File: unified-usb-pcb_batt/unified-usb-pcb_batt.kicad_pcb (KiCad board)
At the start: 2 copper layers, 30 x 35 mm, 38 parts, among them J1 QI, J2 HRO C-31-M-12, J3 USB_Out, J4 BATT, J5 THERM, SW1 SW_SPDT, U1 SRV05-4, U2 DW01A, U3 TP4056, U4 FS8205

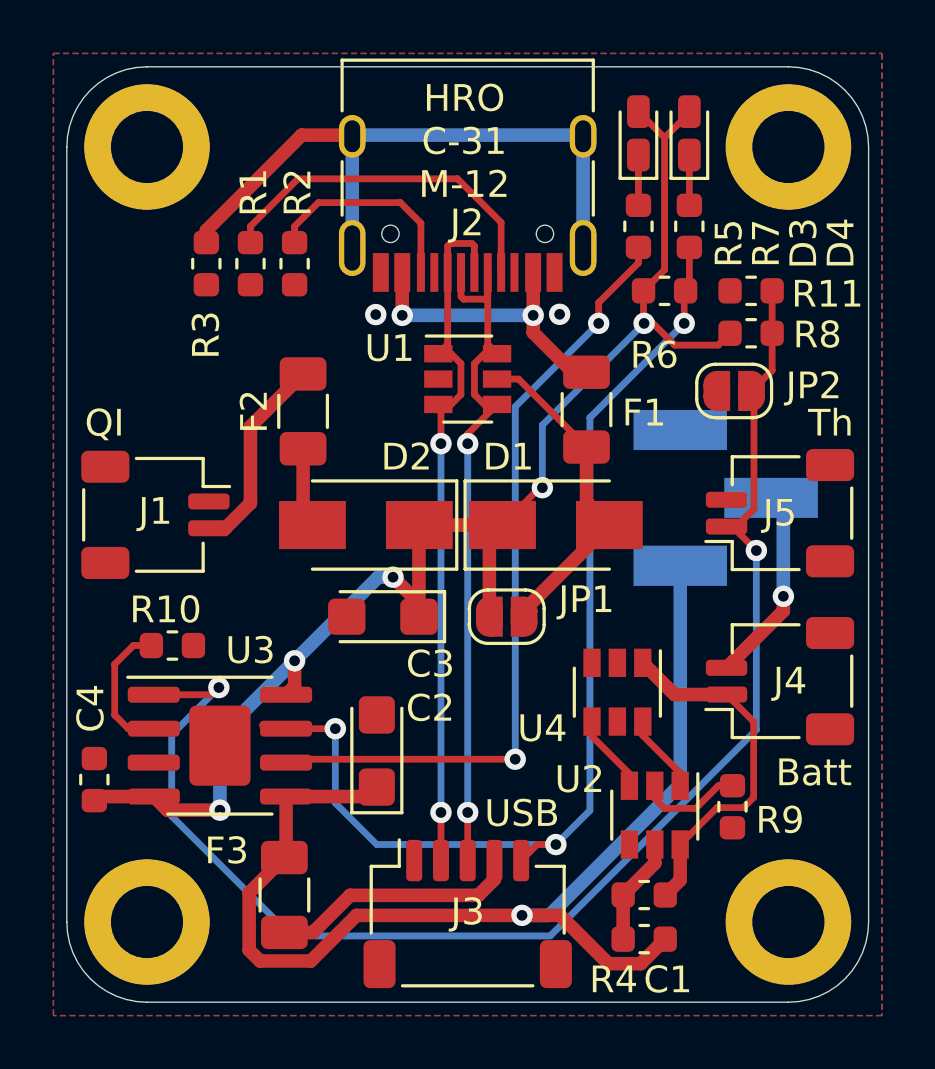
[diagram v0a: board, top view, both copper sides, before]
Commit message: matched usb trace length
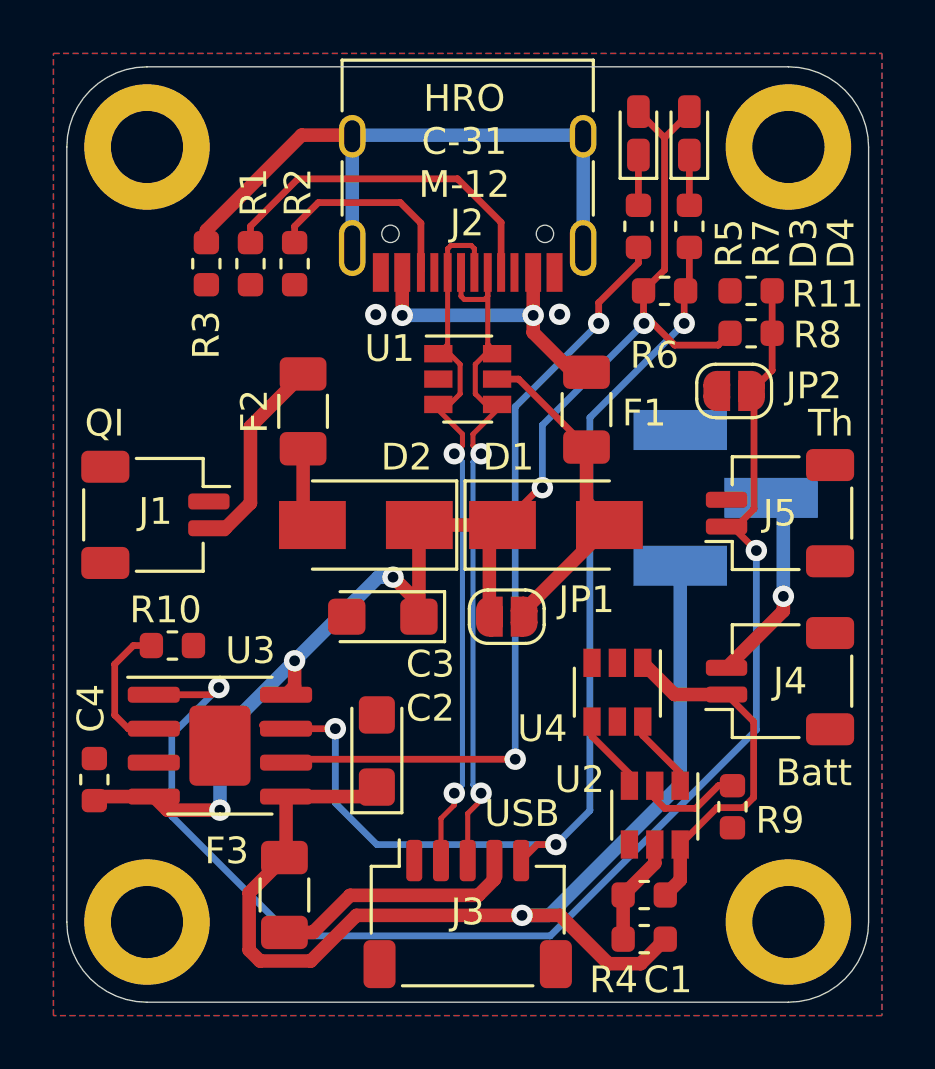
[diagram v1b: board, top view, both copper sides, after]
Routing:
- net USB_D+: track 26.5 -> 27.2 mm
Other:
- net class Default: trace_width 0.254 -> 0.1905
- rule trace_min: 0.2 -> 0.127
- rule via_min_size: 0.4 -> 0.6

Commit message: added ferrite bead
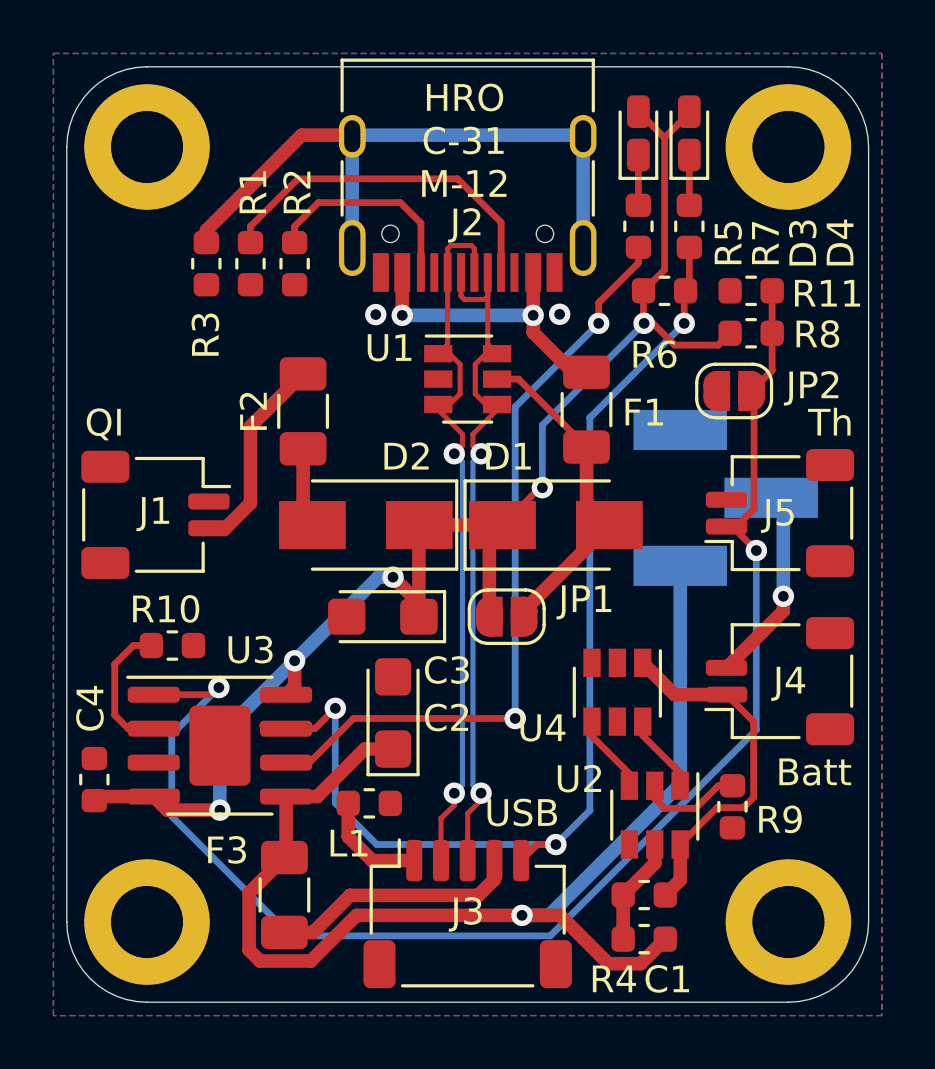
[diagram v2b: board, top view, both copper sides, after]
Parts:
- added L1: BLM18PG121SN1D, Inductor_SMD:L_0603_1608Metric, F.Cu at (27.1, 45.8)
- J2: value HRO C-31-M-12 -> USB_C_Receptacle_USB2.0
- moved C2 1.55 mm to (28.0, 42.5)
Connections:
- J3 pad 1: GNDPWR -> GND
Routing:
- net GND: track 0.00 -> 4.09 mm
- net chgsense: track 39.5 -> 40.6 mm
- net VOUT: track 43.9 -> 44.8 mm
- net Net-(R5-Pad1): track 29.7 -> 29.0 mm
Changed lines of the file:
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@@
     (thickness 1.6)
     (drawings 14)
-    (tracks 229)
+    (tracks 235)
     (zones 0)
-    (modules 38)
-    (nets 32)
+    (modules 39)
+    (nets 33)
   )
   (page A4)
@@
   )
   (setup
-    (last_trace_width 0.1905)
+    (last_trace_width 0.254)
     (user_trace_width 0.254)
     (user_trace_width 0.3048)
@@
   (net 30 "Net-(SW1-Pad1)")
   (net 31 "Net-(J4-Pad2)")
+  (net 32 GND)
   (net_class Default "This is the default net class."
     (clearance 0.1905)
@@
     (diff_pair_width 0.1905)
     (diff_pair_gap 0.2032)
+    (add_net GND)
     (add_net GNDPWR)
     (add_net "Net-(C1-Pad1)")
@@
     (add_net "Net-(F2-Pad2)")
     (add_net "Net-(F3-Pad1)")
+  )
+  (module Inductor_SMD:L_0603_1608Metric (layer F.Cu)
+    (at 27.0764 45.847)
+    (descr "Inductor SMD 0603 (1608 Metric), square (rectangular) end terminal, IPC_7351 nominal, (Body size source: http://www.tortai-tech.com/upload/download/2011102023233369053.pdf), generated with kicad-footprint-generator")
+    (tags inductor)
+    (attr smd)
+    (fp_text reference L1 (at -0.762 1.524) (layer F.SilkS)
+      (effects (font (size 1 1) (thickness 0.15)))
+    )
+    (fp_text value BLM18PG121SN1D (at 0 1.43) (layer F.Fab)
+      (effects (font (size 1 1) (thickness 0.15)))
+    )
+    (fp_text user %R (at 0 0) (layer F.Fab)
+      (effects (font (size 0.4 0.4) (thickness 0.06)))
+    )
+    (fp_line (start 1.48 0.73) (end -1.48 0.73) (layer F.CrtYd) (width 0.05))
+    (fp_line (start 1.48 -0.73) (end 1.48 0.73) (layer F.CrtYd) (width 0.05))
+    (fp_line (start -1.48 -0.73) (end 1.48 -0.73) (layer F.CrtYd) (width 0.05))
+    (fp_line (start -1.48 0.73) (end -1.48 -0.73) (layer F.CrtYd) (width 0.05))
+    (fp_line (start -0.162779 0.51) (end 0.162779 0.51) (layer F.SilkS) (width 0.12))
+    (fp_line (start -0.162779 -0.51) (end 0.162779 -0.51) (layer F.SilkS) (width 0.12))
+    (fp_line (start 0.8 0.4) (end -0.8 0.4) (layer F.Fab) (width 0.1))
+    (fp_line (start 0.8 -0.4) (end 0.8 0.4) (layer F.Fab) (width 0.1))
+    (fp_line (start -0.8 -0.4) (end 0.8 -0.4) (layer F.Fab) (width 0.1))
+    (fp_line (start -0.8 0.4) (end -0.8 -0.4) (layer F.Fab) (width 0.1))
+    (pad 2 smd roundrect (at 0.7875 0) (size 0.875 0.95) (layers F.Cu F.Paste F.Mask) (roundrect_rratio 0.25)
+      (net 3 GNDPWR))
+    (pad 1 smd roundrect (at -0.7875 0) (size 0.875 0.95) (layers F.Cu F.Paste F.Mask) (roundrect_rratio 0.25)
+      (net 32 GND))
+    (model ${KISYS3DMOD}/Inductor_SMD.3dshapes/L_0603_1608Metric.wrl
+      (at (xyz 0 0 0))
+      (scale (xyz 1 1 1))
+      (rotate (xyz 0 0 0))
+    )
   )
   (module Package_TO_SOT_SMD:SOT-23-6 (layer F.Cu)
@@
       (net 16 USB_D+))
     (pad 1 smd roundrect (at -2 -2) (size 0.6 1.55) (layers F.Cu F.Paste F.Mask) (roundrect_rratio 0.25)
-      (net 3 GNDPWR))
+      (net 32 GND))
     (model ${KIPRJMOD}/../3d/SM05B-SRSS-TB.STEP
       (offset (xyz 0 1.27 -0.3048))
@@
       (effects (font (size 1 1) (thickness 0.15)))
     )
-    (fp_text value "HRO C-31-M-12" (at 0 5.1) (layer F.Fab)
+    (fp_text value USB_C_Receptacle_USB2.0 (at 0 5.1) (layer F.Fab)
       (effects (font (size 1 1) (thickness 0.15)))
     )
@@
     (tags "capacitor tantalum")
     (attr smd)
-    (fp_text reference C3 (at -1.778 -1.778) (layer F.SilkS)
+    (fp_text reference C3 (at -2.413 -2.032) (layer F.SilkS)
       (effects (font (size 1 1) (thickness 0.15)))
     )
@@
   )
   (module Capacitor_Tantalum_SMD:CP_EIA-3216-18_Kemet-A (layer F.Cu)
-    (at 27.3594 43.888 90)
+    (at 27.9654 42.465 90)
     (descr "Tantalum Capacitor SMD Kemet-A (3216-18 Metric), IPC_7351 nominal, (Body size from: http://www.kemet.com/Lists/ProductCatalog/Attachments/253/KEM_TC101_STD.pdf), generated with kicad-footprint-generator")
     (tags "capacitor tantalum")
     (attr smd)
-    (fp_text reference C2 (at 1.597 2.003 180) (layer F.SilkS)
+    (fp_text reference C2 (at -0.207 2.032 180) (layer F.SilkS)
       (effects (font (size 1 1) (thickness 0.15)))
     )
@@
   (segment (start 34.0094 27.358701) (end 34.199111 27.548412) (width 0.254) (layer F.Cu) (net 3))
   (segment (start 34.199111 27.548412) (end 34.199111 27.515809) (width 0.254) (layer B.Cu) (net 3))
-  (segment (start 27.1314 45.466) (end 27.3594 45.238) (width 0.508) (layer F.Cu) (net 4))
   (segment (start 23.9014 47.876) (end 22.58189 49.19551) (width 0.508) (layer F.Cu) (net 4))
   (segment (start 22.58189 51.338678) (end 22.988722 51.74551) (width 0.508) (layer F.Cu) (net 4))
@@
   (segment (start 23.9634 47.814) (end 23.9014 47.876) (width 0.508) (layer F.Cu) (net 4))
   (segment (start 23.9634 45.593) (end 23.9634 47.814) (width 0.508) (layer F.Cu) (net 4))
-  (segment (start 27.0044 45.593) (end 27.3594 45.238) (width 0.508) (layer F.Cu) (net 4))
-  (segment (start 23.9634 45.593) (end 27.0044 45.593) (width 0.508) (layer F.Cu) (net 4))
   (segment (start 34.216588 50.038) (end 32.791396 50.038) (width 0.508) (layer F.Cu) (net 4))
   (segment (start 36.025098 51.84651) (end 34.216588 50.038) (width 0.508) (layer F.Cu) (net 4))
   (segment (start 37.23139 51.84651) (end 36.025098 51.84651) (width 0.508) (layer F.Cu) (net 4))
   (segment (start 38.1509 50.927) (end 37.23139 51.84651) (width 0.508) (layer F.Cu) (net 4))
+  (segment (start 26.907906 43.815) (end 27.9654 43.815) (width 0.508) (layer F.Cu) (net 4))
+  (segment (start 25.129906 45.593) (end 26.907906 43.815) (width 0.508) (layer F.Cu) (net 4))
+  (segment (start 23.9634 45.593) (end 25.129906 45.593) (width 0.508) (layer F.Cu) (net 4))
   (segment (start 32.0614 35.433) (end 28.9494 35.433) (width 0.508) (layer F.Cu) (net 5))
   (segment (start 38.1254 20.9426) (end 37.1475 19.9647) (width 0.254) (layer F.Cu) (net 5))
@@
   (segment (start 38.8594 27.888) (end 35.3314 31.416) (width 0.254) (layer B.Cu) (net 20))
   (segment (start 35.3314 31.416) (end 35.3314 46.116) (width 0.254) (layer B.Cu) (net 20))
-  (via (at 25.8064 43.053) (size 0.8) (drill 0.4) (layers F.Cu B.Cu) (net 20))
+  (segment (start 25.8064 45.835) (end 25.8064 42.291) (width 0.254) (layer B.Cu) (net 20))
+  (segment (start 23.9634 43.053) (end 25.0444 43.053) (width 0.254) (layer F.Cu) (net 20))
+  (segment (start 25.0444 43.053) (end 25.8064 42.291) (width 0.254) (layer F.Cu) (net 20))
   (segment (start 27.3594 47.388) (end 25.8064 45.835) (width 0.254) (layer B.Cu) (net 20))
   (segment (start 34.0594 47.388) (end 27.3594 47.388) (width 0.254) (layer B.Cu) (net 20))
-  (segment (start 25.8064 45.835) (end 25.8064 43.053) (width 0.254) (layer B.Cu) (net 20))
-  (segment (start 23.9634 43.053) (end 25.8064 43.053) (width 0.254) (layer F.Cu) (net 20))
+  (via (at 25.8064 42.291) (size 0.8) (drill 0.4) (layers F.Cu B.Cu) (net 20))
   (segment (start 40.81606 35.4885) (end 40.3799 35.4885) (width 0.254) (layer F.Cu) (net 21))
   (segment (start 41.47241 34.83215) (end 40.81606 35.4885) (width 0.254) (layer F.Cu) (net 21))
@@
   (segment (start 35.6594 27.115112) (end 37.1475 25.627012) (width 0.254) (layer F.Cu) (net 22))
   (segment (start 35.6594 27.888) (end 35.6594 27.115112) (width 0.254) (layer F.Cu) (net 22))
-  (via (at 32.537412 44.196) (size 0.8) (drill 0.4) (layers F.Cu B.Cu) (net 22))
-  (segment (start 32.5374 44.195988) (end 32.537412 44.196) (width 0.254) (layer B.Cu) (net 22))
+  (segment (start 23.9634 44.323) (end 24.0904 44.196) (width 0.254) (layer F.Cu) (net 22))
   (segment (start 35.6594 27.888) (end 32.5374 31.01) (width 0.254) (layer B.Cu) (net 22))
-  (segment (start 32.5374 31.01) (end 32.5374 44.195988) (width 0.254) (layer B.Cu) (net 22))
-  (segment (start 24.0904 44.196) (end 32.537412 44.196) (width 0.254) (layer F.Cu) (net 22))
-  (segment (start 23.9634 44.323) (end 24.0904 44.196) (width 0.254) (layer F.Cu) (net 22))
+  (segment (start 32.5374 31.01) (end 32.5374 42.671988) (width 0.254) (layer B.Cu) (net 22))
+  (via (at 32.537412 42.672) (size 0.8) (drill 0.4) (layers F.Cu B.Cu) (net 22))
+  (segment (start 23.9634 44.323) (end 24.836302 44.323) (width 0.254) (layer F.Cu) (net 22))
+  (segment (start 32.5374 42.671988) (end 32.537412 42.672) (width 0.254) (layer B.Cu) (net 22))
+  (segment (start 24.836302 44.323) (end 26.487302 42.672) (width 0.254) (layer F.Cu) (net 22))
+  (segment (start 26.487302 42.672) (end 32.537412 42.672) (width 0.254) (layer F.Cu) (net 22))
   (segment (start 38.130399 46.035501) (end 37.7594 45.664502) (width 0.254) (layer F.Cu) (net 23))
   (segment (start 37.7594 45.664502) (end 37.7594 45.188) (width 0.254) (layer F.Cu) (net 23))
@@
   (via (at 42.5704 38.1) (size 0.8) (drill 0.4) (layers F.Cu B.Cu) (net 31))
   (segment (start 42.5704 38.648) (end 42.5704 38.1) (width 0.508) (layer F.Cu) (net 31))
+  (segment (start 27.1854 47.988) (end 28.7594 47.988) (width 0.508) (layer F.Cu) (net 32))
+  (segment (start 26.2889 45.847) (end 26.2889 47.0915) (width 0.508) (layer F.Cu) (net 32))
+  (segment (start 26.2889 47.0915) (end 27.1854 47.988) (width 0.508) (layer F.Cu) (net 32))
   (zone (net 3) (net_name GNDPWR) (layer F.Cu) (hatch edge 0.508)
     (connect_pads (clearance 0.2032))

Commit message: moved outline/holes for usb-c connector to protrude 1 mm
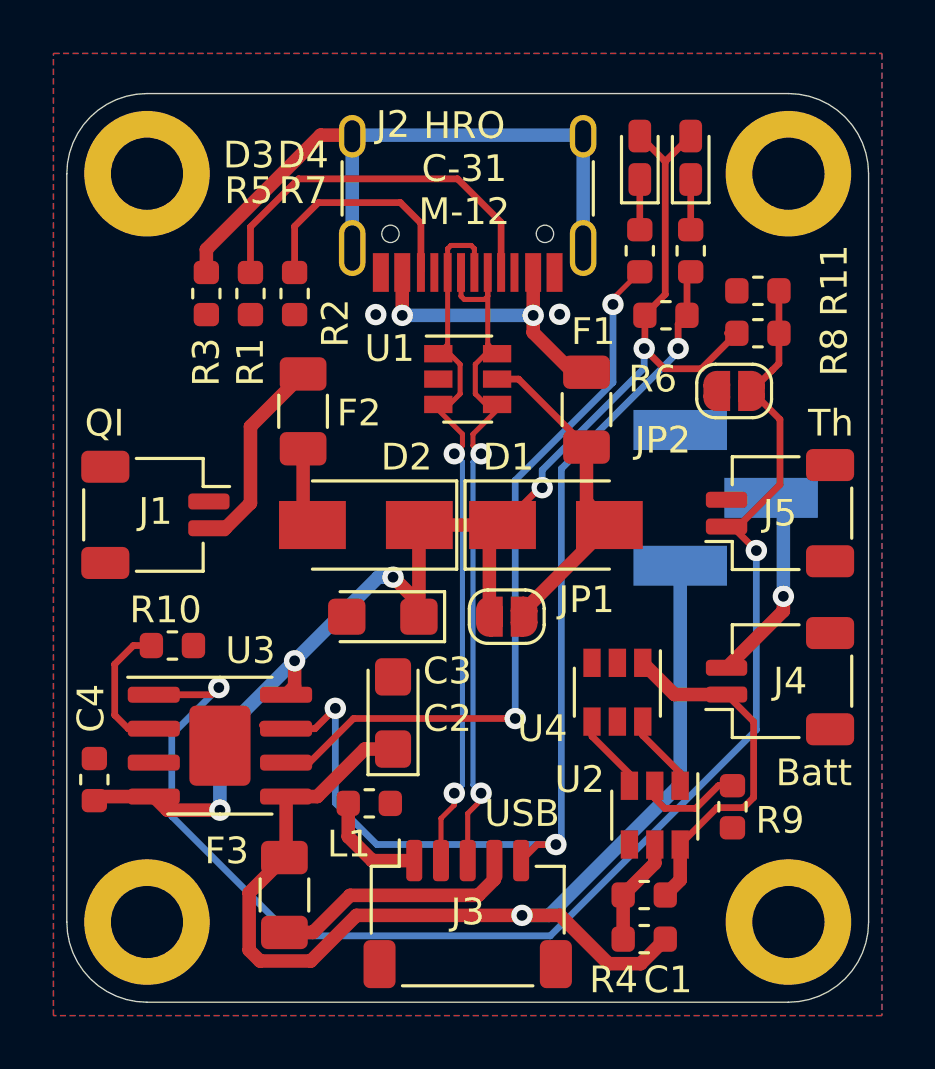
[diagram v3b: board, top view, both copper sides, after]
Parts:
- moved R1 1.12 mm to (22.6, 26.8)
- moved R2 1.12 mm to (24.3, 26.8)
- moved R3 1.12 mm to (21.0, 26.8)
- moved H1 1.00 mm to (18.8, 22.3)
- moved H2 1.00 mm to (42.8, 22.3)
- moved D3 0.92 mm to (37.2, 21.7)
- moved D4 0.92 mm to (39.1, 21.7)
- moved R5 0.92 mm to (37.2, 25.2)
- moved R6 0.92 mm to (38.2, 27.6)
- moved R7 0.92 mm to (39.1, 25.2)
- moved R11 0.25 mm to (41.6, 26.7)
- moved R8 0.25 mm to (41.6, 28.3)
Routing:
- net Net-(J5-Pad1): track 52.7 -> 54.2 mm
- net Net-(J2-PadB5): track 7.83 -> 8.94 mm
- net Net-(J2-PadA5): track 13.2 -> 14.3 mm
- net Net-(R5-Pad1): track 29.0 -> 28.1 mm
- net chgsense: track 40.6 -> 39.7 mm
- net Net-(J2-PadS1): track 24.4 -> 25.1 mm
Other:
- board size 30 x 35 mm -> 30 x 34 mm

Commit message: moved connectors
in order to less obstruct underglow less
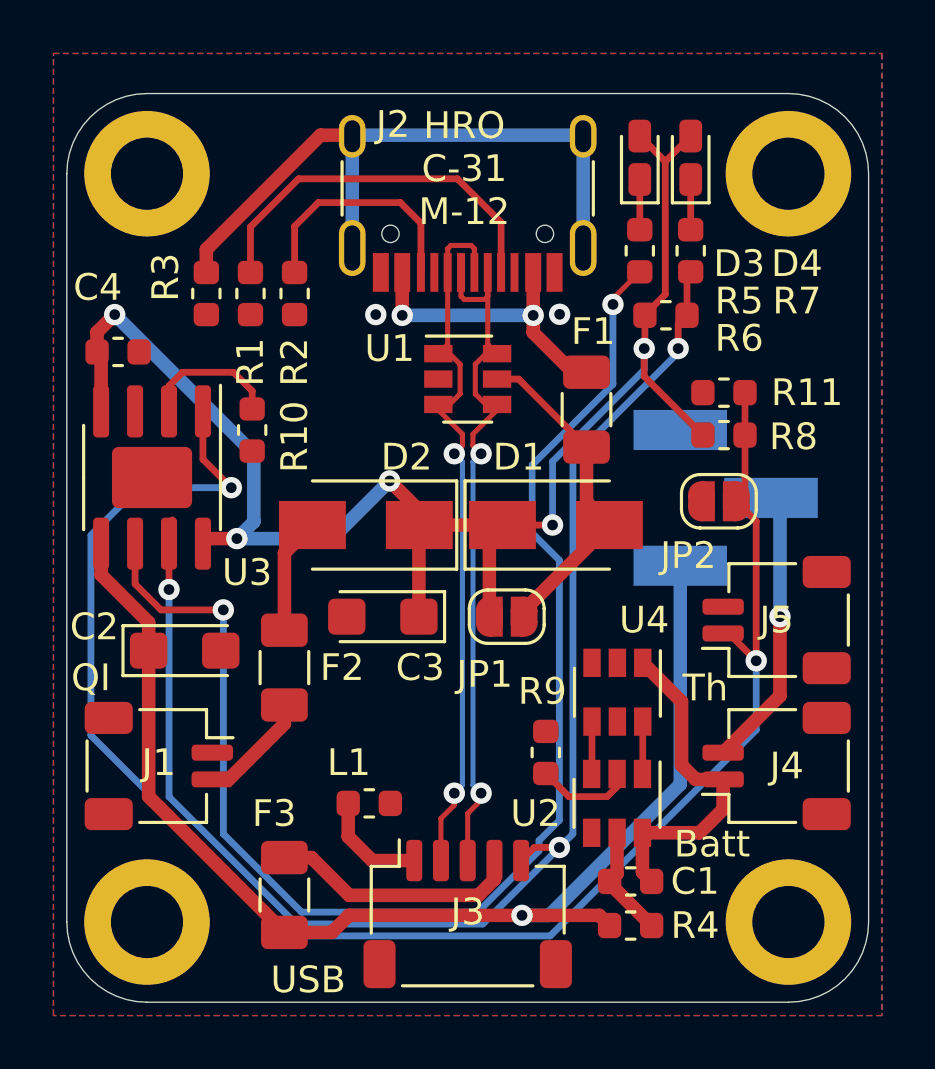
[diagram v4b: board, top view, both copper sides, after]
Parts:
- moved C4 16.0 mm to (17.7, 29.0), turned to 0 degrees
- moved U3 10.3 mm to (18.9, 33.7), turned to 270 degrees
- moved F2 9.61 mm to (23.9, 40.8), turned to 270 degrees
- moved J1 9.40 mm to (19.2, 44.5)
- moved R10 8.60 mm to (22.7, 31.9), turned to 90 degrees
- moved C2 8.14 mm to (20.2, 40.1), turned to 0 degrees
- moved R9 7.27 mm to (33.7, 43.9), turned to 270 degrees
- moved JP2 4.17 mm to (40.2, 34.5)
- moved R8 4.02 mm to (40.3, 32.1)
- moved R11 4.02 mm to (40.3, 30.5)
- moved J5 4.00 mm to (42.3, 39.0)
- moved J4 3.18 mm to (42.3, 44.5)
- moved U2 1.48 mm to (36.3, 45.8)
- moved C1 0.72 mm to (36.9, 48.8)
- moved R4 0.72 mm to (36.9, 50.4), turned to 180 degrees
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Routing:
- net Net-(R5-Pad1): track 28.1 -> 52.7 mm
- net chgsense: track 39.7 -> 52.5 mm
- net Net-(J5-Pad1): track 54.2 -> 62.7 mm
- net +5V: track 53.5 -> 59.1 mm
- net Net-(J4-Pad2): track 7.43 -> 11.2 mm
- net Net-(F2-Pad2): track 7.59 -> 4.26 mm
- net Net-(D2-Pad2): track 3.00 -> 4.86 mm
- net VOUT: track 44.8 -> 46.1 mm
- net Net-(U2-Pad1): track 2.98 -> 1.96 mm
- net Net-(U2-Pad3): track 2.98 -> 1.96 mm
- net Net-(C1-Pad2): track 13.5 -> 12.7 mm
